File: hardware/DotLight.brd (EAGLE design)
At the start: 25.4 x 45.7 mm, 21 parts, among them Q1 BSH103, Q2 BSH103

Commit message: v0.2.1
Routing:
- net TXD: track 30.1 -> 35.3 mm
- net RXD: track 44.4 -> 45.4 mm
- net TOUCH_EMIT: track 57.2 -> 58.2 mm
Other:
- board text added: "v0.2.1"
- board text removed: "v0.2.0"
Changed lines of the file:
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@@
 <setting verticaltext="up"/>
 </settings>
-<grid distance="1" unitdist="mil" unit="mil" style="lines" multiple="1" display="yes" altdistance="0.0025" altunitdist="inch" altunit="inch"/>
+<grid distance="1" unitdist="mil" unit="mm" style="lines" multiple="1" display="yes" altdistance="0.0025" altunitdist="inch" altunit="inch"/>
 <layers>
 <layer number="1" name="Top" color="4" fill="1" visible="yes" active="yes"/>
@@
 <layer number="14" name="Route14" color="1" fill="6" visible="no" active="no"/>
 <layer number="15" name="Route15" color="4" fill="6" visible="no" active="yes"/>
-<layer number="16" name="Bottom" color="1" fill="1" visible="no" active="yes"/>
+<layer number="16" name="Bottom" color="1" fill="1" visible="yes" active="yes"/>
 <layer number="17" name="Pads" color="2" fill="1" visible="yes" active="yes"/>
 <layer number="18" name="Vias" color="2" fill="1" visible="yes" active="yes"/>
-<layer number="19" name="Unrouted" color="6" fill="1" visible="no" active="yes"/>
+<layer number="19" name="Unrouted" color="6" fill="1" visible="yes" active="yes"/>
 <layer number="20" name="Dimension" color="15" fill="1" visible="yes" active="yes"/>
 <layer number="21" name="tPlace" color="7" fill="1" visible="yes" active="yes"/>
@@
 <wire x1="26.234921875" y1="46.160209375" x2="26.229840625" y2="14.696390625" width="0" layer="20"/>
 <dimension x1="-8.26314375" y1="2.548390625" x2="-8.26314375" y2="30.488390625" x3="-3.18314375" y3="16.518390625" textsize="1.778" layer="48"/>
-<text x="2.720071875" y="35.5336375" size="1.016" layer="21" rot="SR270" align="center">v0.2.0</text>
+<text x="2.720071875" y="35.5336375" size="1.016" layer="21" rot="SR270" align="center">v0.2.1</text>
 <dimension x1="24.00611875" y1="32.03465" x2="23.95785625" y2="0.820390625" x3="39.385971875" y3="16.4037" textsize="1.778" layer="48"/>
 <dimension x1="0.380475" y1="0.79325" x2="25.8120625" y2="0.80006875" x3="13.098325" y3="-6.87395" textsize="1.778" layer="48"/>
@@
 <wire x1="15.0876" y1="32.1564" x2="13.716" y2="32.1564" width="0.1524" layer="16"/>
 <wire x1="15.24" y1="32.004" x2="15.0876" y2="32.1564" width="0.1524" layer="16"/>
-<wire x1="15.24" y1="30.1752" x2="15.24" y2="32.004" width="0.1524" layer="16"/>
-<wire x1="14.1732" y1="29.1084" x2="15.24" y2="30.1752" width="0.1524" layer="16"/>
 <wire x1="11.2776" y1="29.1084" x2="14.1732" y2="29.1084" width="0.1524" layer="16"/>
 <wire x1="1.9812" y1="38.4048" x2="11.2776" y2="29.1084" width="0.1524" layer="16"/>
@@
 <wire x1="8.382" y1="24.5364" x2="8.4" y2="24.42" width="0.1524" layer="1"/>
 <wire x1="1.9812" y1="44.5008" x2="1.974715625" y2="44.58476875" width="0.1524" layer="1"/>
+<wire x1="15.24" y1="32.004" x2="15.24" y2="31.0134" width="0.1524" layer="16"/>
+<wire x1="15.24" y1="31.0134" x2="15.0876" y2="30.861" width="0.1524" layer="16"/>
+<wire x1="15.0876" y1="30.861" x2="14.732" y2="30.861" width="0.1524" layer="16"/>
+<wire x1="14.732" y1="30.861" x2="14.5796" y2="30.7086" width="0.1524" layer="16"/>
+<wire x1="14.5796" y1="30.7086" x2="14.5796" y2="29.5148" width="0.1524" layer="16"/>
+<wire x1="14.5796" y1="29.5148" x2="14.1732" y2="29.1084" width="0.1524" layer="16"/>
 </signal>
 <signal name="MISO">
@@
 <contactref element="JP1" pad="3"/>
 <contactref element="U$1" pad="5"/>
-<wire x1="15.24" y1="32.4612" x2="15.6972" y2="32.4612" width="0.1524" layer="16"/>
-<wire x1="14.6304" y1="33.0708" x2="15.24" y2="32.4612" width="0.1524" layer="16"/>
-<wire x1="14.6304" y1="33.9852" x2="14.6304" y2="33.0708" width="0.1524" layer="16"/>
-<wire x1="14.1732" y1="34.4424" x2="14.6304" y2="33.9852" width="0.1524" layer="16"/>
 <wire x1="14.1732" y1="35.6616" x2="14.1732" y2="34.4424" width="0.1524" layer="1"/>
 <wire x1="15.6972" y1="37.1856" x2="14.1732" y2="35.6616" width="0.1524" layer="1"/>
@@
 <wire x1="15.6972" y1="32.4612" x2="15.7176" y2="32.401" width="0.1524" layer="16"/>
 <wire x1="19.6596" y1="44.5008" x2="19.754715625" y2="44.58476875" width="0.1524" layer="16"/>
-<via x="14.1732" y="34.4424" extent="1-16" drill="0.3"/>
 <via x="18.288" y="42.5196" extent="1-16" drill="0.3"/>
+<wire x1="15.6972" y1="32.4612" x2="15.6972" y2="32.3342" width="0.1524" layer="16"/>
+<wire x1="15.6972" y1="32.3342" x2="16.3322" y2="31.6992" width="0.1524" layer="16"/>
+<wire x1="16.3322" y1="31.6992" x2="16.3322" y2="31.1404" width="0.1524" layer="16"/>
+<wire x1="16.3322" y1="31.1404" x2="15.4178" y2="30.3276" width="0.1524" layer="16"/>
+<via x="15.4178" y="30.3276" extent="1-16" drill="0.3"/>
+<wire x1="15.4178" y1="30.3276" x2="14.4526" y2="30.3276" width="0.1524" layer="1"/>
+<wire x1="14.4526" y1="30.3276" x2="14.1478" y2="30.6324" width="0.1524" layer="1"/>
+<wire x1="14.1478" y1="30.6324" x2="14.1478" y2="34.417" width="0.1524" layer="1"/>
+<wire x1="14.1478" y1="34.417" x2="14.1732" y2="34.4424" width="0.1524" layer="1"/>
 </signal>
 <signal name="SCK">
@@
 <wire x1="16.002" y1="32.9184" x2="15.8496" y2="32.9184" width="0.1524" layer="16"/>
 <wire x1="16.3068" y1="32.6136" x2="16.002" y2="32.9184" width="0.1524" layer="16"/>
-<wire x1="16.3068" y1="30.7848" x2="16.3068" y2="32.6136" width="0.1524" layer="16"/>
-<wire x1="14.3256" y1="28.8036" x2="16.3068" y2="30.7848" width="0.1524" layer="16"/>
-<wire x1="10.668" y1="28.8036" x2="14.3256" y2="28.8036" width="0.1524" layer="16"/>
+<wire x1="10.668" y1="28.8036" x2="14.4272" y2="28.8036" width="0.1524" layer="16"/>
 <wire x1="9.144" y1="30.3276" x2="10.668" y2="28.8036" width="0.1524" layer="16"/>
 <wire x1="12.954" y1="30.3276" x2="9.144" y2="30.3276" width="0.1524" layer="1"/>
@@
 <via x="24.384" y="38.862" extent="1-16" drill="0.3"/>
 <via x="23.4696" y="43.1292" extent="1-16" drill="0.3"/>
+<wire x1="16.3068" y1="32.6136" x2="16.5862" y2="32.6136" width="0.1524" layer="16"/>
+<wire x1="16.5862" y1="32.6136" x2="17.018" y2="32.1818" width="0.1524" layer="16"/>
+<wire x1="17.018" y1="32.1818" x2="17.018" y2="31.0388" width="0.1524" layer="16"/>
+<wire x1="14.4272" y1="28.8036" x2="14.8336" y2="29.21" width="0.1524" layer="16"/>
+<wire x1="14.8336" y1="29.21" x2="15.1892" y2="29.21" width="0.1524" layer="16"/>
+<wire x1="15.1892" y1="29.21" x2="17.018" y2="31.0388" width="0.1524" layer="16"/>
 </signal>
 <signal name="VIN_PIN">
@@
 <wire x1="5.6388" y1="27.5844" x2="5.6388" y2="26.9748" width="0.1524" layer="16"/>
 <wire x1="6.5532" y1="28.4988" x2="5.6388" y2="27.5844" width="0.1524" layer="16"/>
-<wire x1="14.478" y1="28.4988" x2="6.5532" y2="28.4988" width="0.1524" layer="16"/>
-<wire x1="16.6116" y1="30.6324" x2="14.478" y2="28.4988" width="0.1524" layer="16"/>
-<wire x1="16.6116" y1="33.0708" x2="16.6116" y2="30.6324" width="0.1524" layer="16"/>
-<wire x1="16.1544" y1="33.528" x2="16.6116" y2="33.0708" width="0.1524" layer="16"/>
+<wire x1="14.9606" y1="28.4988" x2="6.5532" y2="28.4988" width="0.1524" layer="16"/>
 <wire x1="20.4216" y1="19.5072" x2="20.47" y2="19.628" width="0.1524" layer="1"/>
 <via x="17.2212" y="36.4236" extent="1-16" drill="0.3"/>
@@
 <via x="17.723559375" y="21.619359375" extent="1-16" drill="0.3"/>
 <via x="1.83371875" y="15.7043625" extent="1-16" drill="0.3"/>
+<wire x1="16.1544" y1="33.528" x2="17.4498" y2="32.2326" width="0.1524" layer="16"/>
+<wire x1="17.4498" y1="32.2326" x2="17.4498" y2="31.0134" width="0.1524" layer="16"/>
+<wire x1="17.4498" y1="31.0134" x2="14.9606" y2="28.4988" width="0.1524" layer="16"/>
 </signal>
 <signal name="TOUCH_SENSE">

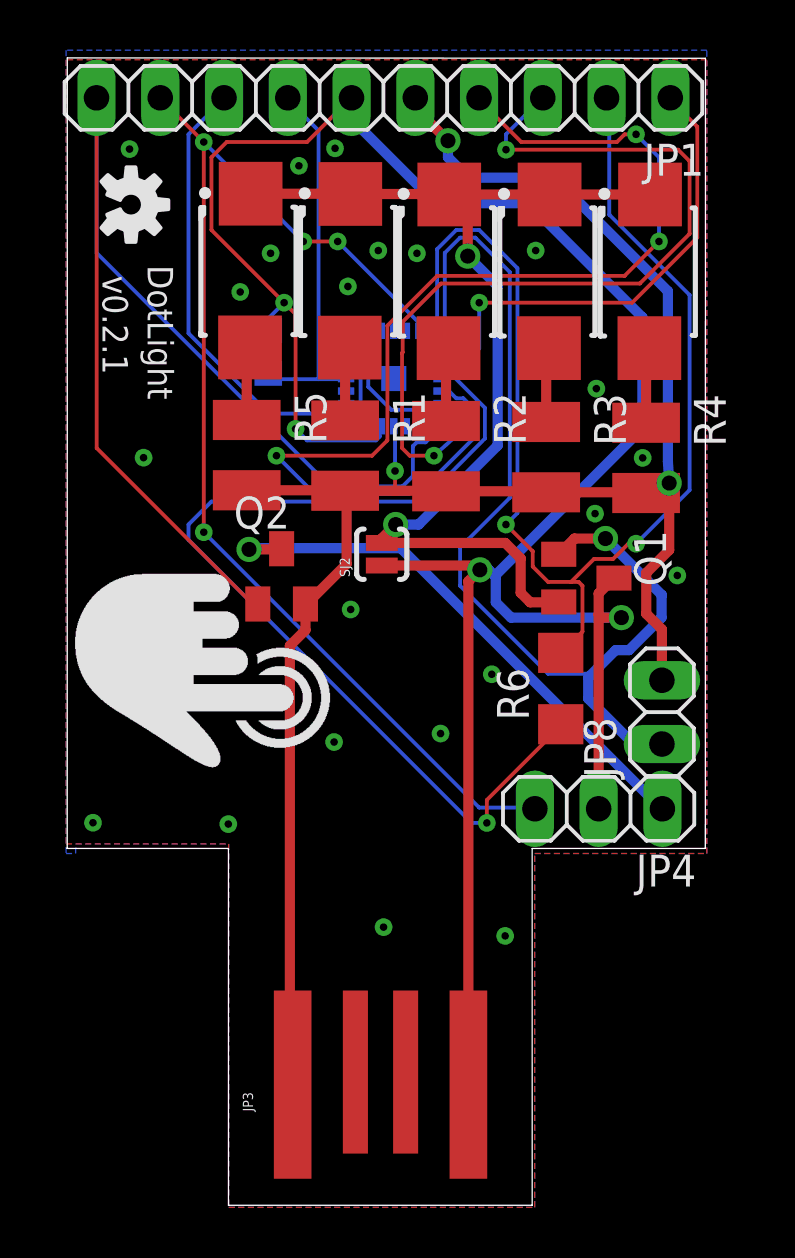
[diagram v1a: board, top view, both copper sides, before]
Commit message: Add RGB led
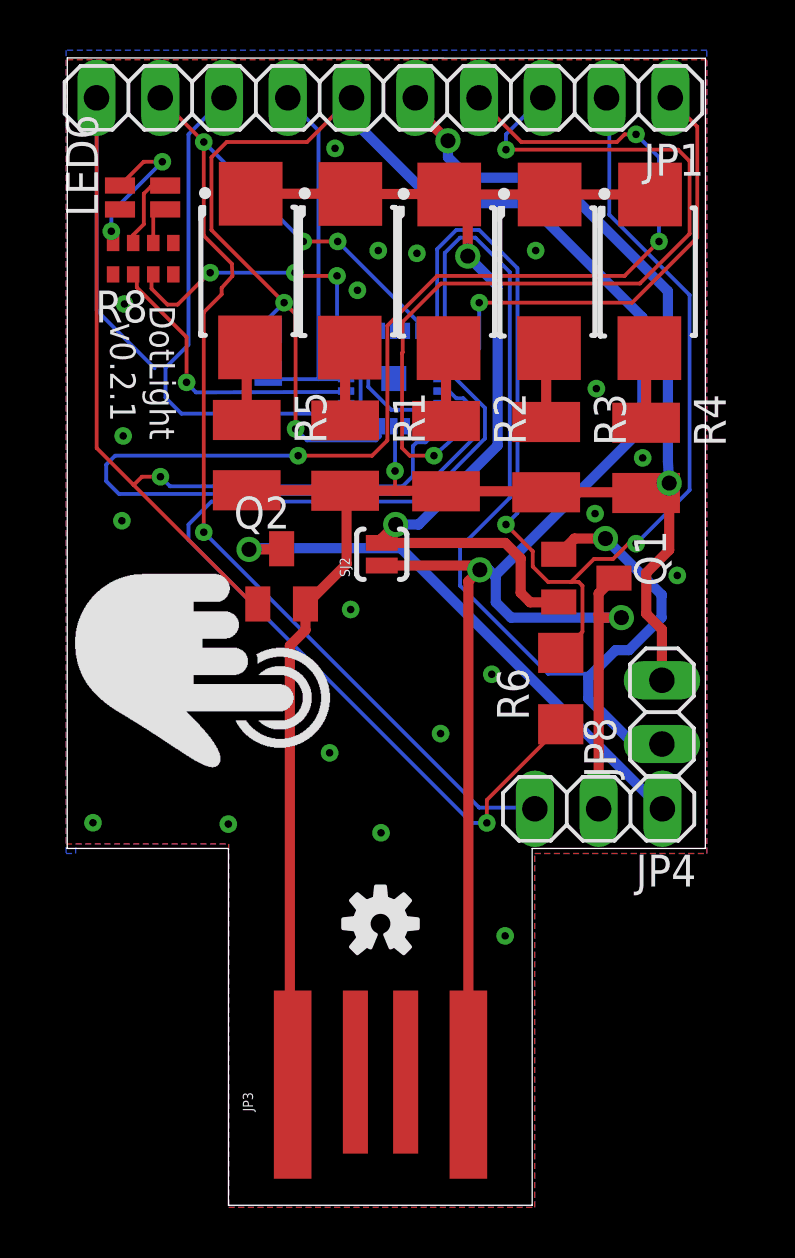
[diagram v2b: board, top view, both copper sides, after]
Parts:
- added LED6: GM1WA55311A, led:GM1WA55311A
- added R8: 4.7kΩ, SparkFun:0603-ARV
- moved LOGO1 30.3 mm to (13.3, 11.7), turned to 0 degrees
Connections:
- new net BLUE: R8.3, U$1.15
- new net GREEN: R8.2, U$1.12
- new net N$1: LED6.2, R8.6
- new net N$2: LED6.3, R8.7
- new net N$4: LED6.1, R8.8
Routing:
- net RXD: track 45.4 -> 59.4 mm
- net BLUE: track 0.00 -> 12.1 mm, vias 0 -> 3
- net GREEN: track 0.00 -> 11.7 mm, vias 0 -> 1
- net N$4: track 0.00 -> 6.19 mm, vias 0 -> 2
- net N$2: track 0.00 -> 3.12 mm
- net SCK: track 20.4 -> 23.2 mm
- net N$1: track 0.00 -> 1.81 mm
- net MISO: track 47.6 -> 48.6 mm
- net MOSI: track 53.9 -> 54.4 mm, vias 0 -> 1
- net TOUCH_EMIT: vias 24 -> 22
